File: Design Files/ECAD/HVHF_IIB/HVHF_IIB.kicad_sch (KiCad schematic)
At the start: 64 parts, among them J1 1984963, J2 1984963, J3 731375003, J4 CONSMA002-L, Q1 PNP, Q2 BFP196E6327HTSA1, T1 BFU590G, T10 BFQ252, T11 BFQ252, T12 BFQ252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

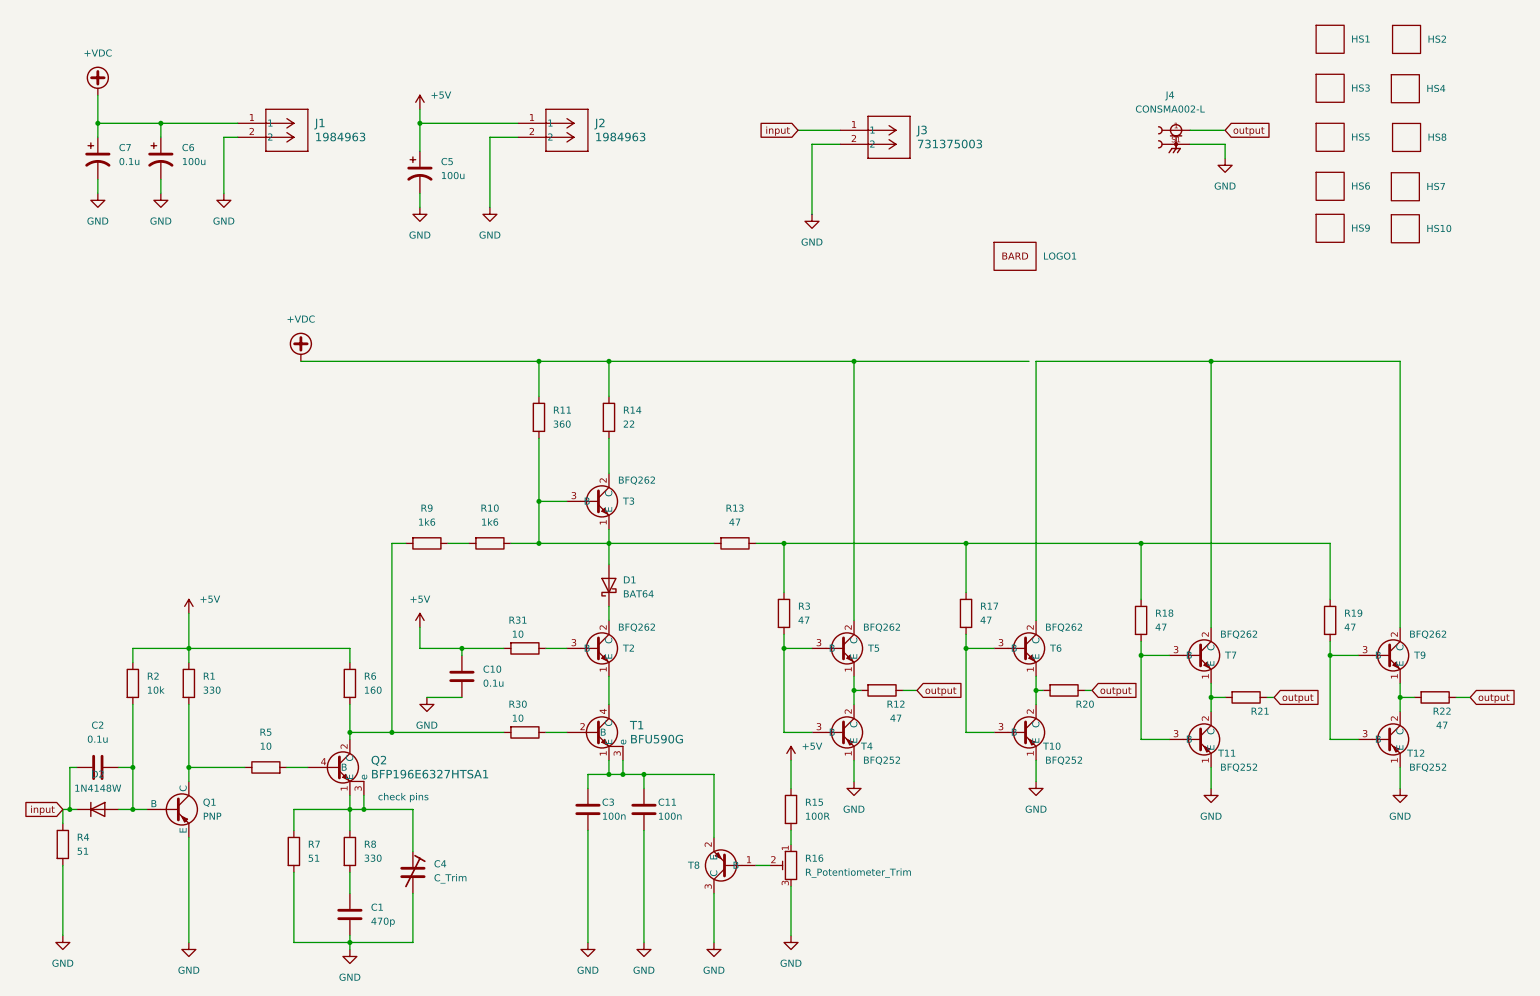
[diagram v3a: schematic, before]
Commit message: board layout
sourced all components
laid out all components
designed all 3D models
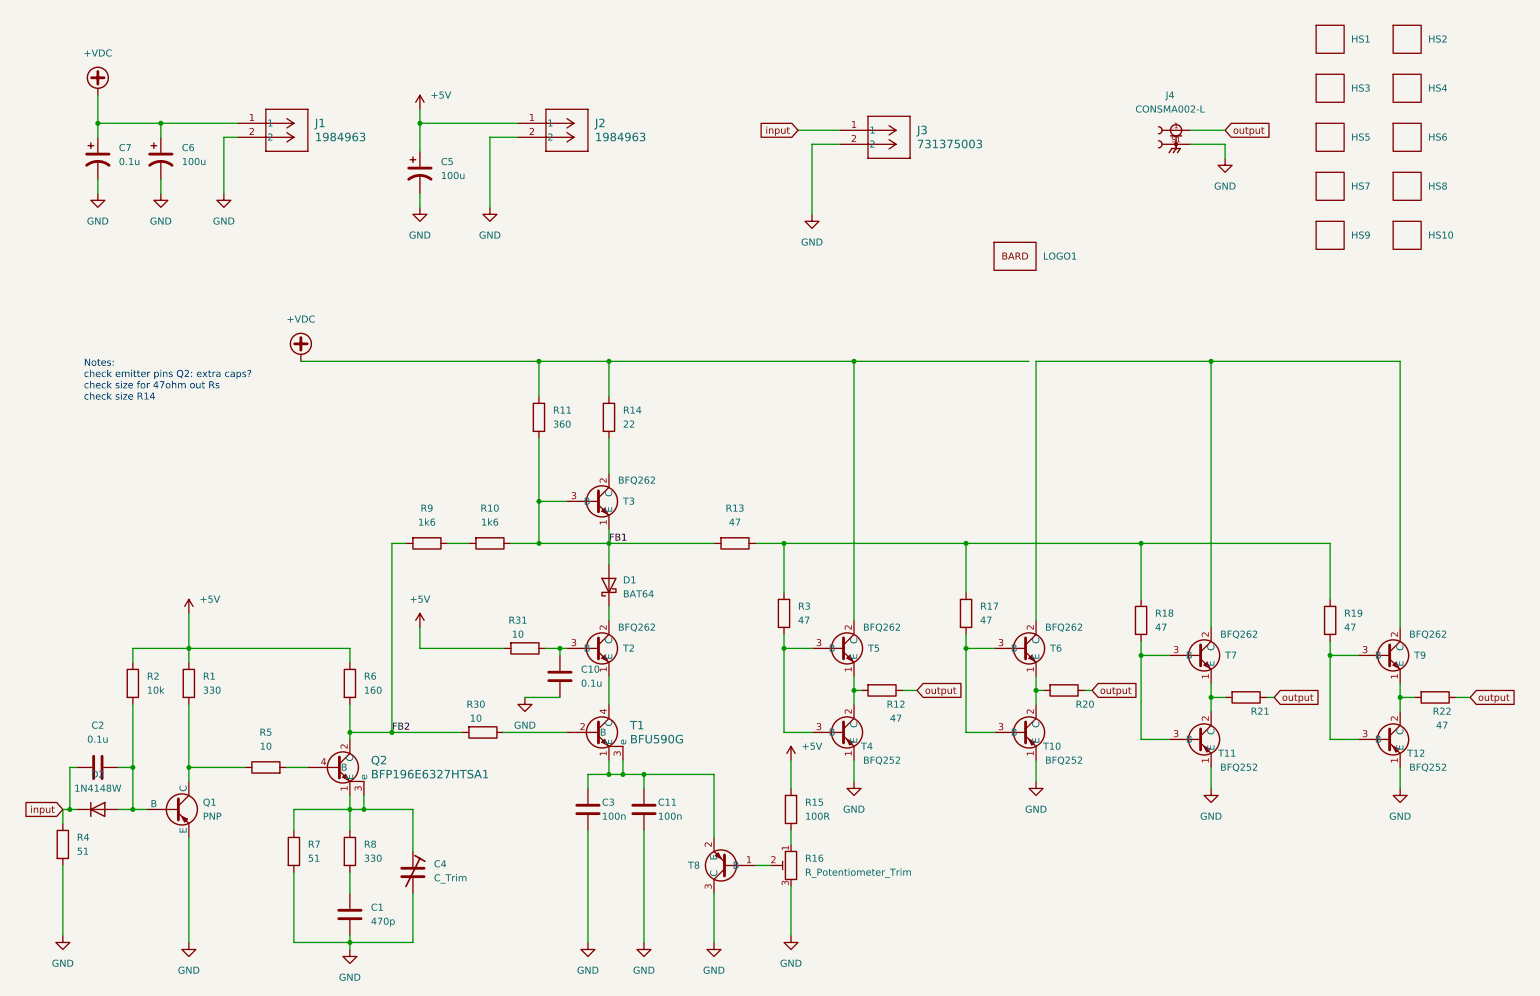
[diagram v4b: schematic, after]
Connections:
- net +5V: no longer C10.1
- net FB2: now reaches Q2.2 (C), R30.2, R6.2, R9.2
- net FB1: now reaches D1.2 (A), R10.1, R11.2, R13.2, T3.1 (E), T3.3 (B)
- net at R31.1, T2.3 (B): now also C10.1
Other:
- note added: "Notes: check emitter pins Q2: extra caps? check size for 47ohm out Rs check size R14"
- note removed: "check pins"
- moved on the sheet: C10, R30

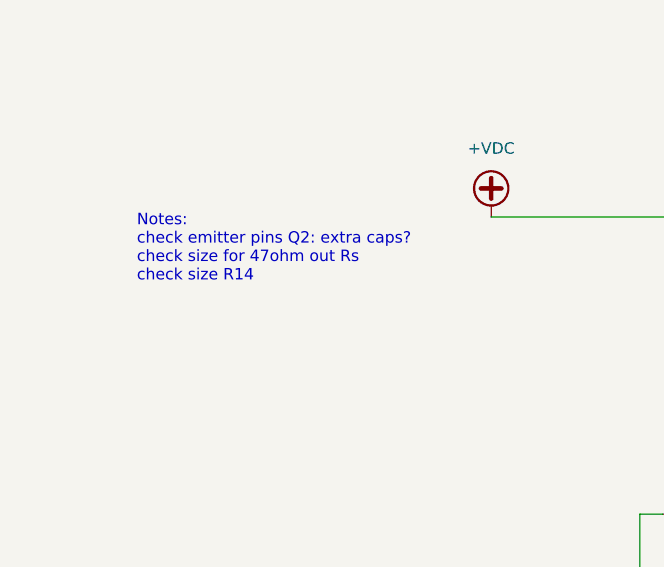
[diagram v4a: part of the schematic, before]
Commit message: fixed Kicad error
board already open error
moved log files to Miscellaneous folder
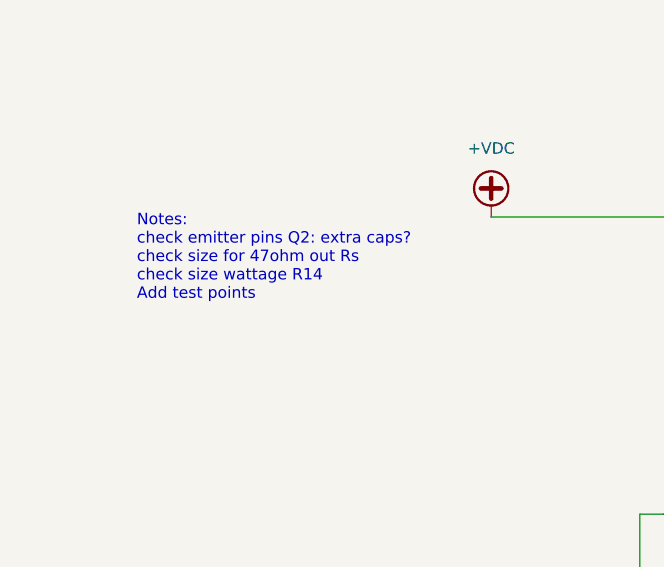
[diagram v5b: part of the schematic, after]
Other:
- note added: "Notes: check emitter pins Q2: extra caps? check size for 47ohm out Rs check size wattage R14 Add test points"
- note removed: "Notes: check emitter pins Q2: extra caps? check size for 47ohm out Rs check size R14"
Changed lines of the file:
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@@
     (stroke (width 0) (type default))
   )
-  (text "Notes:\ncheck emitter pins Q2: extra caps?\ncheck size for 47ohm out Rs\ncheck size R14\n\n\n"
+  (text "Notes:\ncheck emitter pins Q2: extra caps?\ncheck size for 47ohm out Rs\ncheck size wattage R14\nAdd test points\n\n"
     (at 24.13 92.71 0)
     (effects (font (size 1.27 1.27)) (justify left bottom))

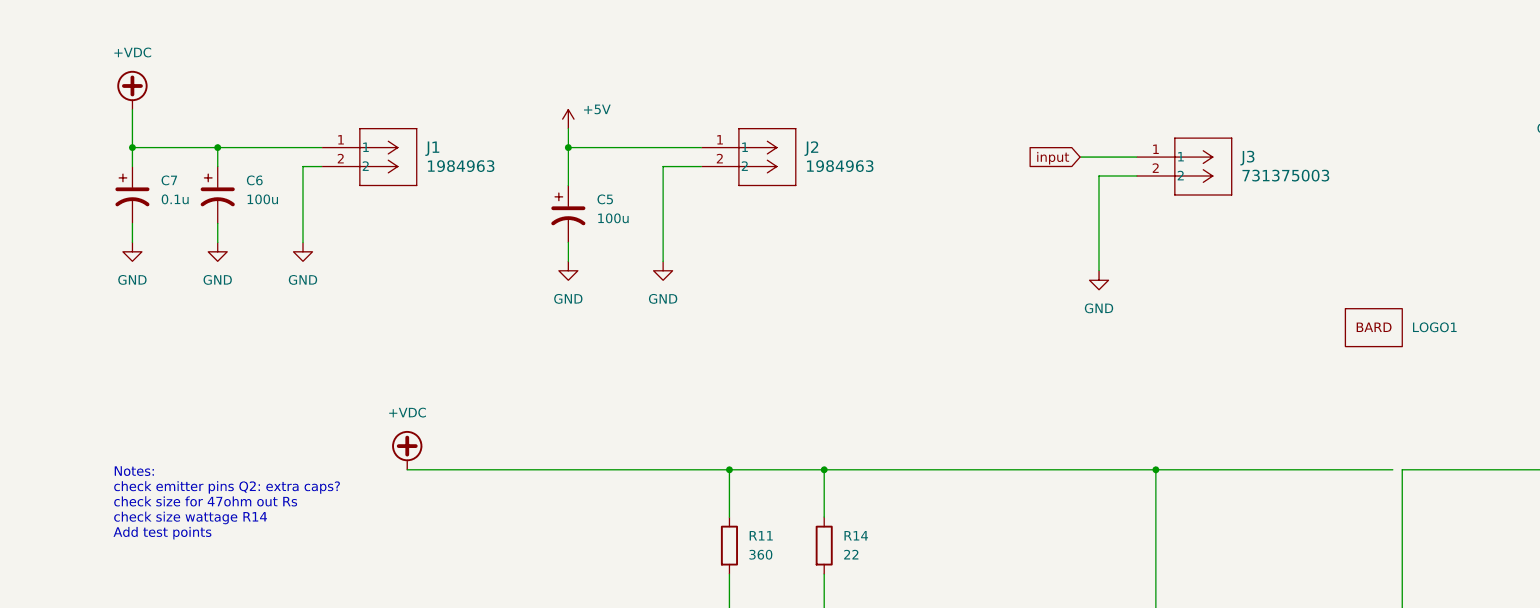
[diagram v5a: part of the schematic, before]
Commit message: pcb work
routing
components
3d models
net classes
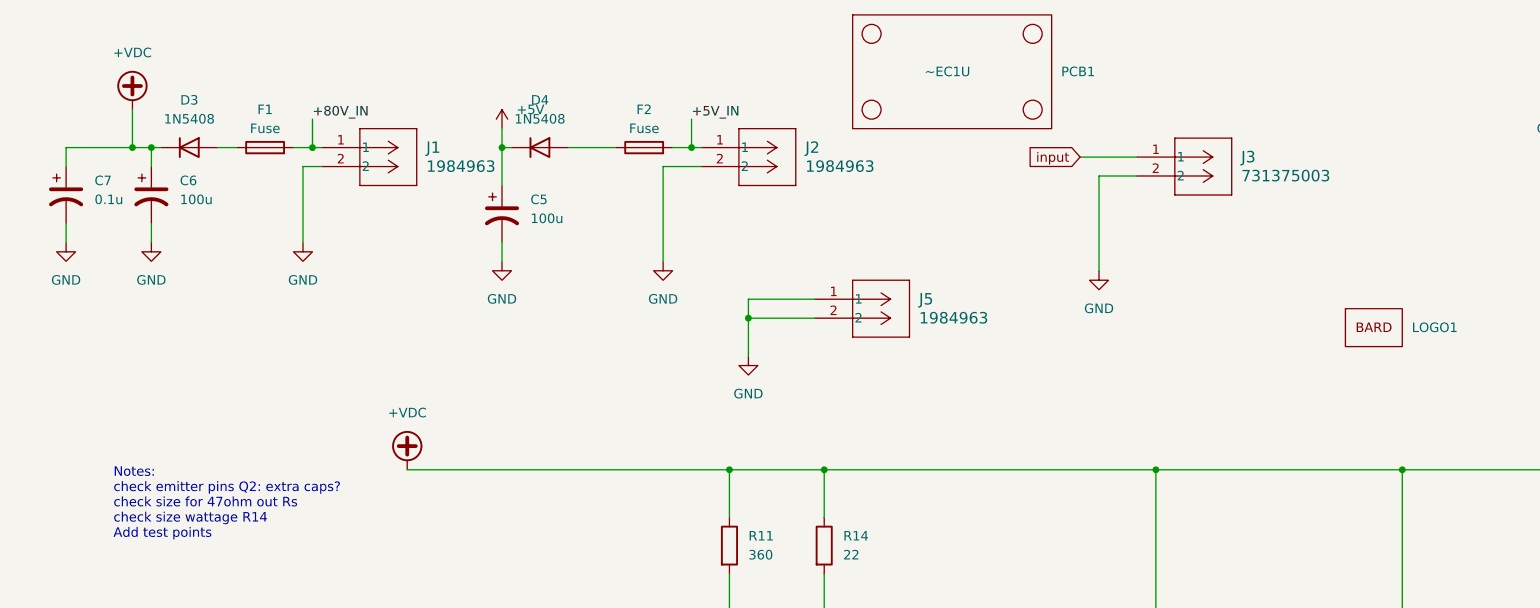
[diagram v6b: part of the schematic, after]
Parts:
- added D3, D4: 1N5408, Diode_THT:D_DO-201AD_P15.24mm_Horizontal, symbol Diode:1N5408
- added F1, F2: Fuse, Library:FUSE_4527, symbol Device:Fuse
- added J5: 1984963, CONN_1984963, symbol New_Library:1984963
- added PCB1: ~EC1U, Library:PCB_EC1U, symbol 1_my_custom_sym_library:PCB_Symbol
- R12, R20, R21, R22: footprint Resistor_SMD:R_0805_2012Metric_Pad1.20x1.40mm_HandSolder -> Library:RES_3560_TEC
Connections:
- net +5V: now also D4.1 (K); no longer J2.1
- net +VDC: now also T6.2 (C), T7.2 (C), T9.2 (C), D3.1 (K); no longer J1.1
- net GND: now also J5.1, J5.2
- new net: D3.2 (A), F1.1
- new net: D4.2 (A), F2.1
- new net +5V_IN: F2.2, J2.1
- new net +80V_IN: F1.2, J1.1
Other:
- moved on the sheet: C5, C6, C7

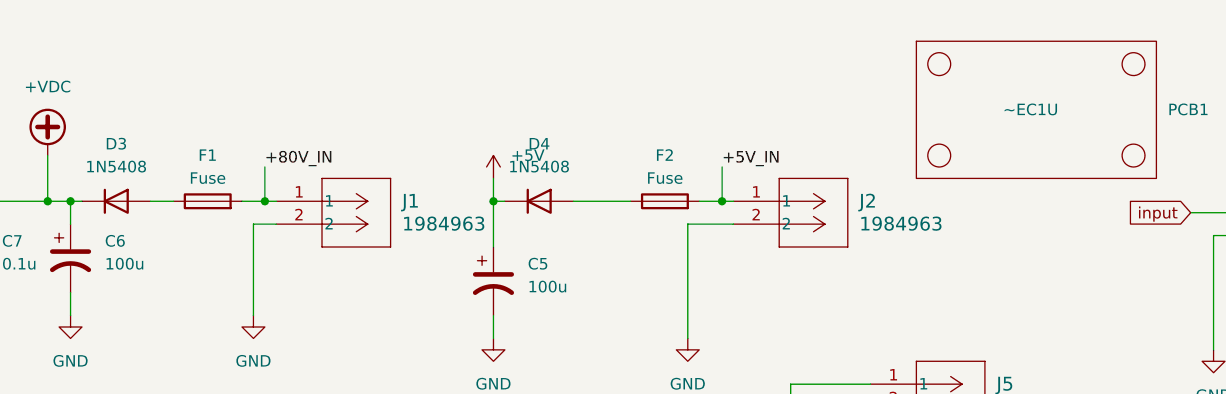
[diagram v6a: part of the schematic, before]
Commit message: pcb routing
routing
updated pcb brd footprint
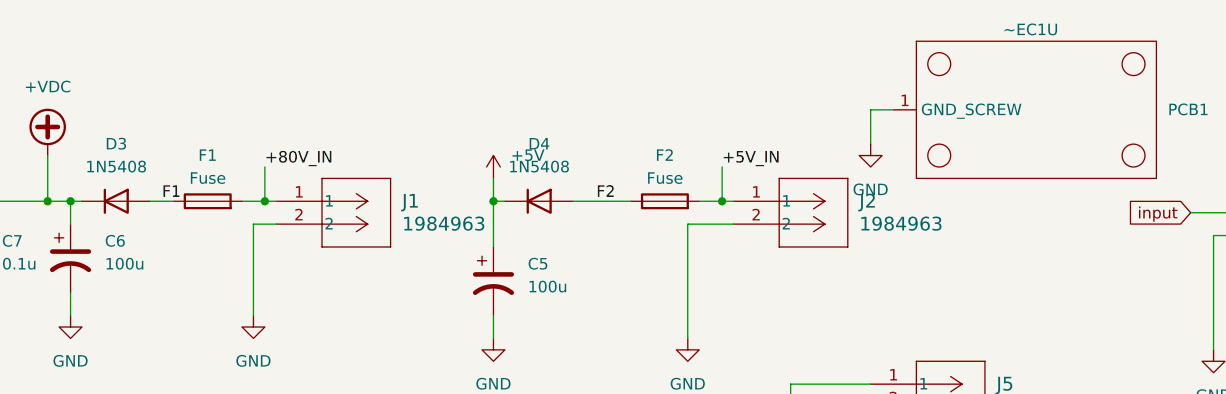
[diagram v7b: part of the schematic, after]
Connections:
- net GND: now also PCB1.1 (GND_SCREW)
- net F1: now reaches D3.2 (A), F1.1
- net F2: now reaches D4.2 (A), F2.1
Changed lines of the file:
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@@
+    (stroke (width 0) (type default))
+  )
+  (wire (pts (xy 118.11 31.75) (xy 118.11 27.94))
     (stroke (width 0) (type default))
   )
@@
   )
   (wire (pts (xy 76.2 35.56) (xy 76.2 38.1))
+    (stroke (width 0) (type default))
+  )
+  (wire (pts (xy 118.11 27.94) (xy 120.65 27.94))
     (stroke (width 0) (type default))
   )
@@
   (text "Notes:\ncheck emitter pins Q2: extra caps?\ncheck size for 47ohm out Rs\ncheck size wattage R14\nAdd test points\n\n"
     (at 24.13 92.71 0)
+    (effects (font (size 1.27 1.27)) (justify left bottom))
+  )
+  (label "F1" (at 39.37 38.1 0) (fields_autoplaced)
+    (effects (font (size 1.27 1.27)) (justify left bottom))
+  )
+  (label "F2" (at 87.63 38.1 0) (fields_autoplaced)
     (effects (font (size 1.27 1.27)) (justify left bottom))
   )
@@
     )
   )
+  (symbol (lib_id "power:GND") (at 118.11 31.75 0) (unit 1)
+    (in_bom yes) (on_board yes) (dnp no) (fields_autoplaced)
+    (property "Reference" "#PWR027" (at 118.11 38.1 0)
+      (effects (font (size 1.27 1.27)) hide)
+    )
+    (property "Value" "GND" (at 118.11 36.83 0)
+      (effects (font (size 1.27 1.27)))
+    )
+    (property "Footprint" "" (at 118.11 31.75 0)
+      (effects (font (size 1.27 1.27)) hide)
+    )
+    (property "Datasheet" "" (at 118.11 31.75 0)
+      (effects (font (size 1.27 1.27)) hide)
+    )
+    (pin "1")
+    (instances
+      (project "HVHF_IIB"
+        (path "/a4785c7b-64d4-4462-915b-801e602c6997"
+          (reference "#PWR027") (unit 1)
+        )
+      )
+    )
+  )
   (symbol (lib_id "Device:R") (at 234.95 142.24 270) (unit 1)
     (in_bom yes) (on_board yes) (dnp no)
@@
   )
   (symbol (lib_id "1_my_custom_sym_library:PCB_Symbol") (at 135.89 27.94 0) (unit 1)
-    (in_bom yes) (on_board yes) (dnp no) (fields_autoplaced)
+    (in_bom yes) (on_board yes) (dnp no)
     (property "Reference" "PCB1" (at 151.13 27.94 0)
       (effects (font (size 1.27 1.27)) (justify left))
     )
-    (property "Value" "~EC1U" (at 135.89 27.94 0)
+    (property "Value" "~EC1U" (at 135.89 19.05 0)
       (effects (font (size 1.27 1.27)))
     )
@@
       (effects (font (size 1.27 1.27)) hide)
     )
-    (instances
-      (project "HVHF_IIB"
+    (pin "1")
+    (instances
+      (project "HVHF_IIB"
